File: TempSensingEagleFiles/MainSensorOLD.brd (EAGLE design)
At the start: 36.5 x 33 mm, 9 parts, among them U3 MLX90614_

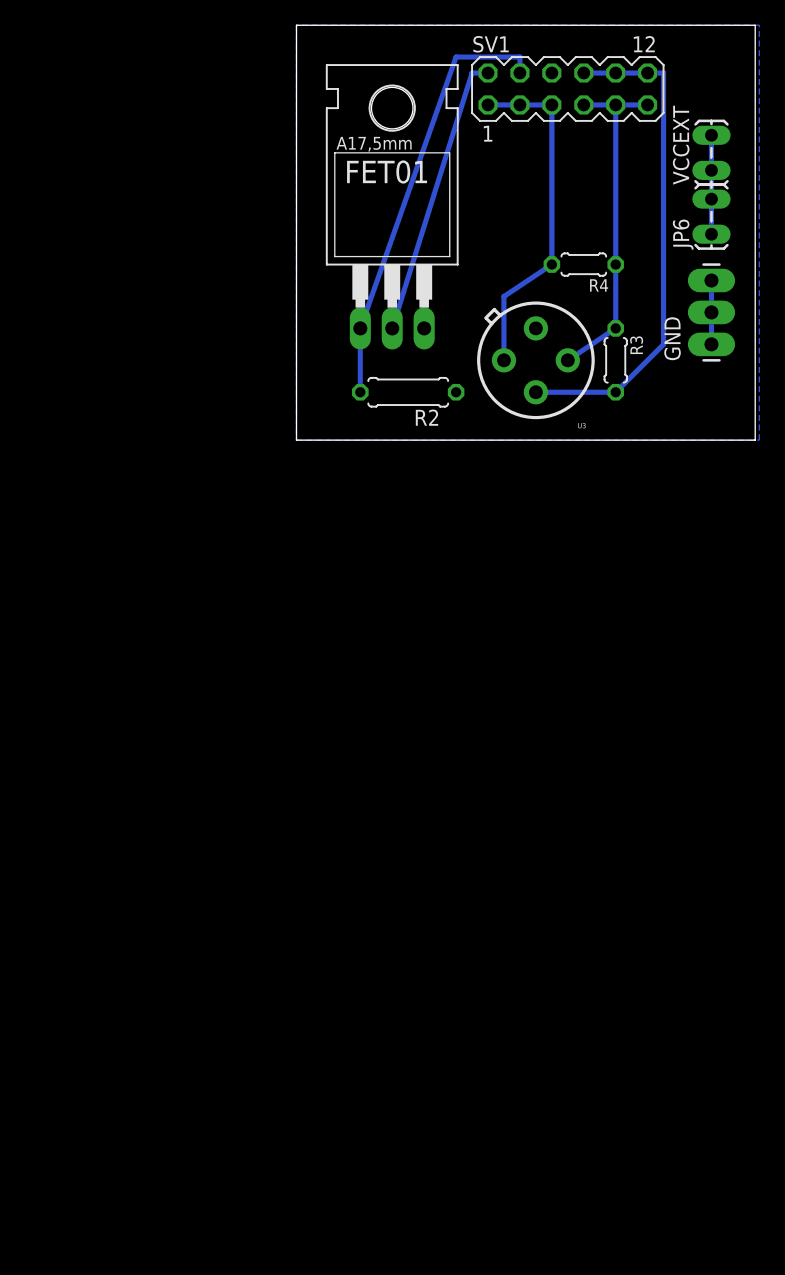
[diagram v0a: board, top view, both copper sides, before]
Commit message: worked on Eagle Files
Added 1 Sensor and Main board
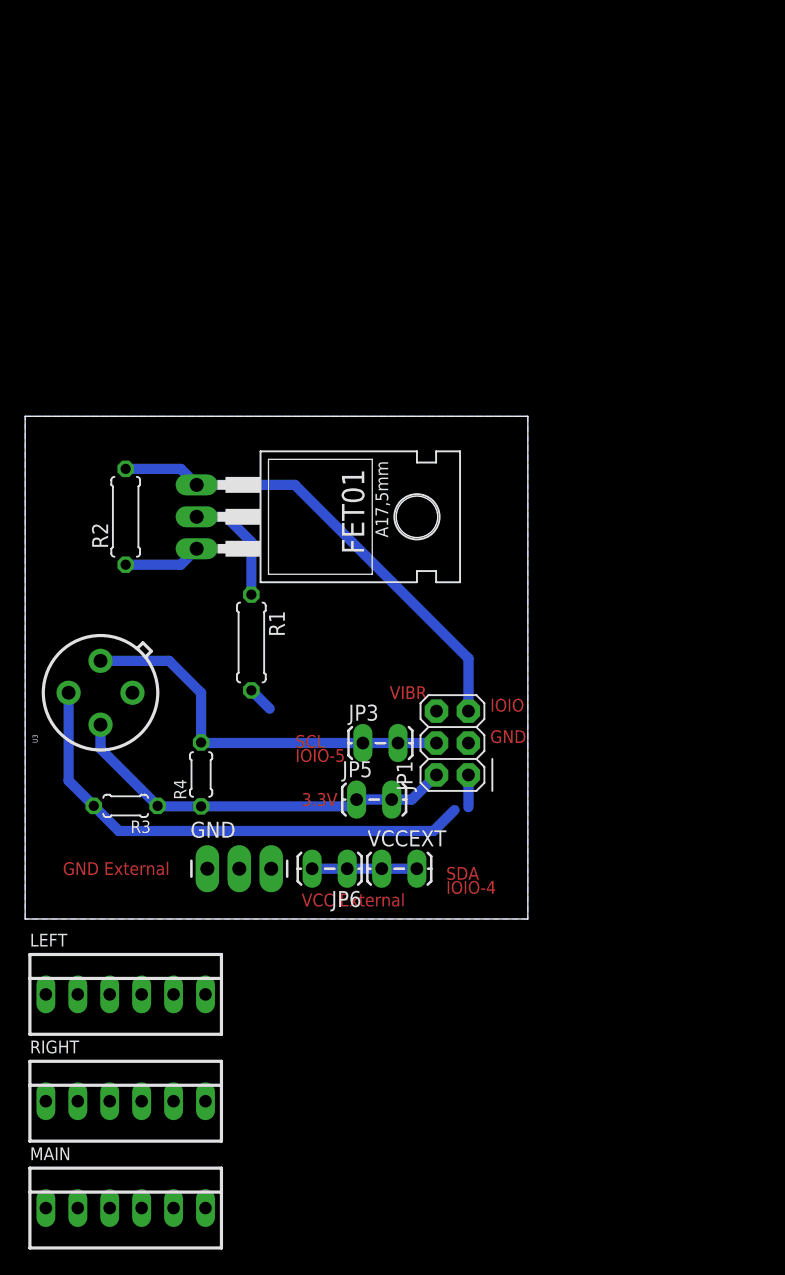
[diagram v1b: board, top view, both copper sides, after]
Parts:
- removed SV1: (no value), con-lstb:MA06-2
- added JP1: (no value), SparkFun-Connectors:2X03
- added JP3, JP5: (no value), SparkFun-Connectors:1X02_LOCK_LONGPADS
- added LEFT, MAIN, RIGHT: (no value), con-molex:22-23-2061
- added R1: 10h, rcl:0207/7
- moved VCCEXT 61.5 mm to (28.5, 4.00), turned to 0 degrees
- moved JP6 58.4 mm to (25.5, 4.00), turned to 180 degrees
- moved GND 57.9 mm to (14.5, 4.00), turned to 0 degrees
- moved R3 52.7 mm to (8.00, 9.00), turned to 180 degrees
- moved R4 50.7 mm to (14.0, 11.5), turned to 90 degrees
- moved U3 43.6 mm to (6.00, 18.0), turned to 90 degrees
- moved R2 24.6 mm to (8.00, 32.0), turned to 90 degrees
- moved FET01 23.2 mm to (20.0, 32.0), turned to 270 degrees
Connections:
- new net N$3: JP1.6, R1.2
- net GND: now also JP1.3
- net N$15: now also JP1.4, JP3.1, JP3.2; no longer SV1.1, SV1.3, SV1.5
- net N$16: now also JP1.1, LEFT.6, RIGHT.1; no longer SV1.10, SV1.12, SV1.8
- net N$18: now also JP1.5; no longer SV1.4
- net N$2: now also R1.1; no longer SV1.2
- net VCC3: now also JP1.2, JP5.1, JP5.2; no longer SV1.11, SV1.7, SV1.9
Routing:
- net N$2: track 22.6 -> 9.37 mm
- net VCC3: track 27.4 -> 32.2 mm
- net N$15: track 27.4 -> 31.8 mm
- net N$18: track 34.3 -> 37.7 mm
- net N$16: track 39.7 -> 42.6 mm
- net N$3: track 0.00 -> 2.33 mm
- net GND: track 5.08 -> 6.46 mm
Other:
- board size 36.5 x 33 mm -> 40 x 40 mm
- board text added: "3.3V"
- board text added: "GND"
- board text added: "GND External"
- board text added: "IOIO"
- board text added: "SCL IOIO-5"
- board text added: "SDA IOIO-4"
- board text added: "VCC External"
- board text added: "VIBR"
